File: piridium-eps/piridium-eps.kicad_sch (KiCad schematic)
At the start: 33 parts

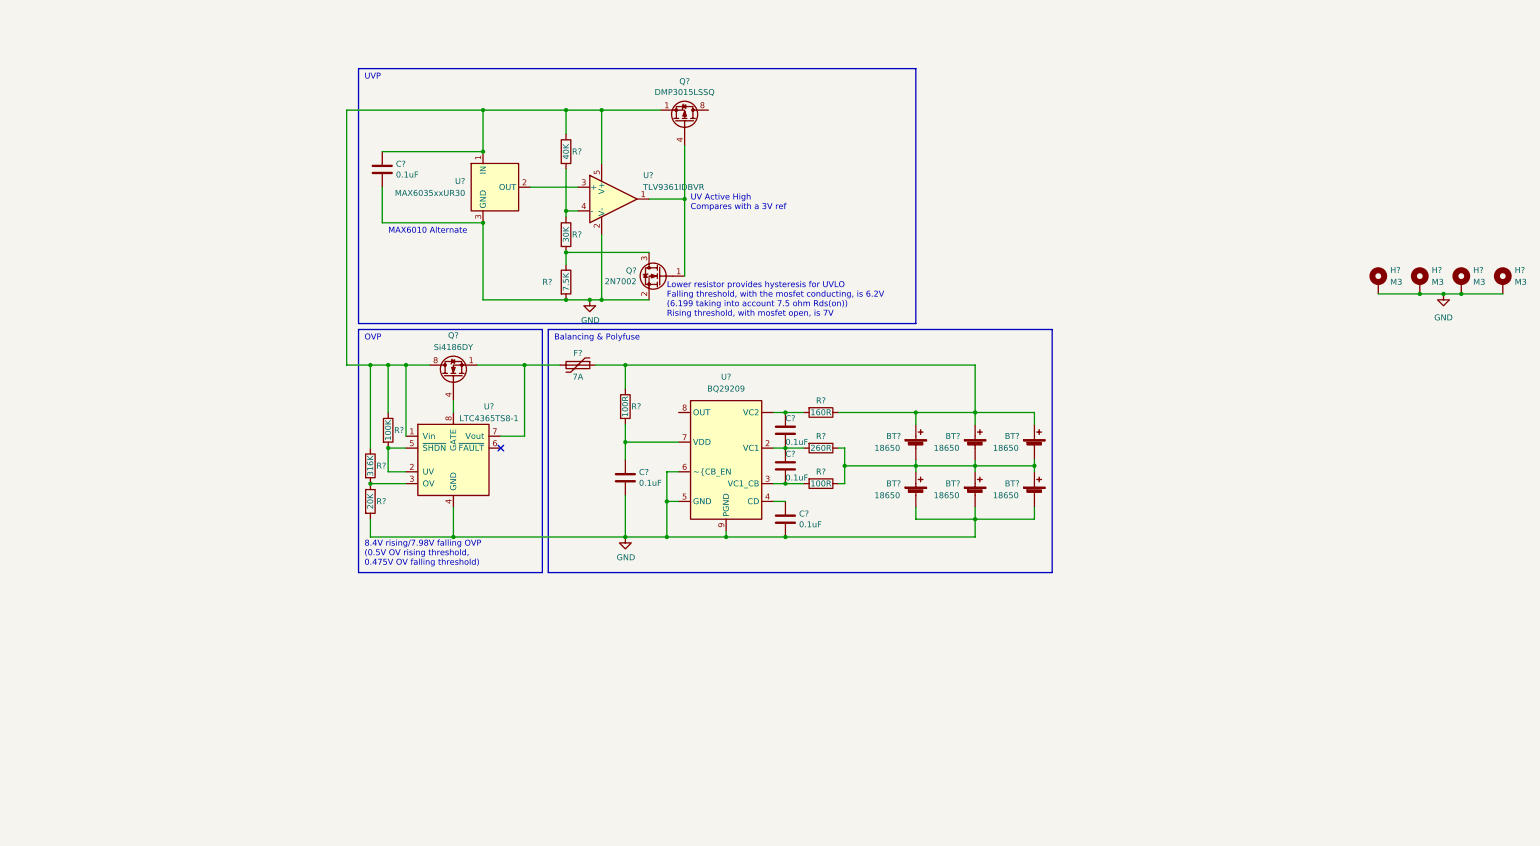
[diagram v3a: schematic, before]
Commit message: add R5460 and small bom edits
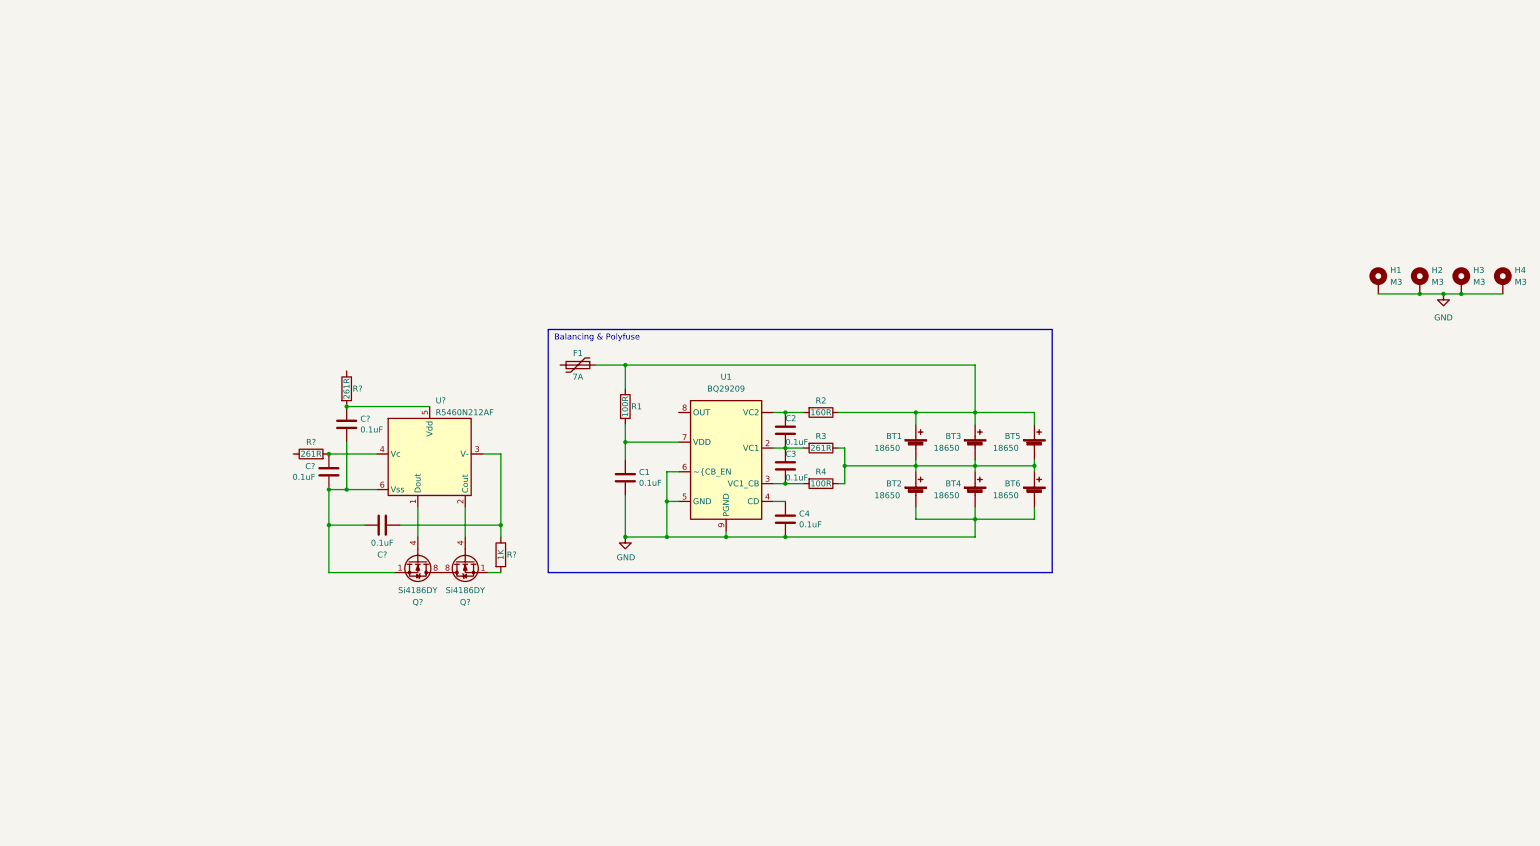
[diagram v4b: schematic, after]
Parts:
- removed C?: 0.1uF, Capacitor_SMD:C_0805_2012Metric, symbol Device:C
- removed Q?: 2N7002, Package_TO_SOT_SMD:SOT-23, symbol Transistor_FET:2N7002
- removed Q?: DMP3015LSSQ, Package_SO:SOIC-8_3.9x4.9mm_P1.27mm, symbol Transistor_FET:IRF7404
- removed Q?: Si4186DY, Package_SO:SOIC-8_3.9x4.9mm_P1.27mm, symbol Transistor_FET:Si4162DY
- removed R?: 30K, Resistor_SMD:R_0805_2012Metric, symbol Device:R
- removed R?: 7.5K, Resistor_SMD:R_0805_2012Metric, symbol Device:R
- removed R?: 100K, Resistor_SMD:R_0805_2012Metric, symbol Device:R
- removed R?: 40K, Resistor_SMD:R_0805_2012Metric, symbol Device:R
- removed R?: 316K, Resistor_SMD:R_0805_2012Metric, symbol Device:R
- removed R?: 20K, Resistor_SMD:R_0805_2012Metric, symbol Device:R
- removed U?: LTC4365TS8-1, Package_TO_SOT_SMD:TSOT-23-8, symbol Power_Management:LTC4365TS8-1
- removed U?: MAX6035xxUR30, Package_TO_SOT_SMD:SOT-23, symbol Reference_Voltage:MAX6035xxUR30
- removed U?: TLV9361IDBVR, Package_TO_SOT_SMD:SOT-23-5, symbol Amplifier_Operational:OPA842xDBV
- added C? (x3): 0.1uF, Capacitor_SMD:C_0805_2012Metric, symbol Device:C
- added Q? (x2): Si4186DY, Package_SO:SOIC-8_3.9x4.9mm_P1.27mm, symbol Transistor_FET:Si4162DY
- added R?: 1K, Resistor_SMD:R_0805_2012Metric, symbol Device:R
- added R? (x2): 261R, Resistor_SMD:R_0805_2012Metric, symbol Device:R
- added U?: R5460N212AF, Package_TO_SOT_SMD:SOT-23-6, symbol piridium-eps:R5460N212AF
- R3: renamed from R?; value 260R -> 261R
- gave numbers to parts that had none: 19
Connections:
- new net: C?.1, R?.2, U?.4 (Vc)
- new net: C?.1, C?.2, C?.2, Q?.1 (S), Q?.2 (S), Q?.3 (S), U?.6 (Vss)
- new net: C?.2, R?.1, U?.3 (V-)
- new net: Q?.1 (S), Q?.2 (S), Q?.3 (S), R?.2
- new net: C?.1, R?.2, U?.5 (Vdd)
- new net: Q?.4 (G), U?.1 (Dout)
- new net: Q?.5 (D), Q?.5 (D), Q?.6 (D), Q?.6 (D), Q?.7 (D), Q?.7 (D), Q?.8 (D), Q?.8 (D)
- new net: Q?.4 (G), U?.2 (Cout)
- no-connect marks 1 -> 0
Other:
- note removed: "8.4V rising/7.98V falling OVP (0.5V OV rising threshold, 0.475V OV falling threshold)"
- note removed: "Lower resistor provides hysteresis for UVLO Falling threshold, with the mosfet conducting, is 6.2V (6.199 taking into account 7.5 ohm Rds(on)) Rising threshold, with mosfet open, is 7V"
- note removed: "MAX6010 Alternate"
- note removed: "OVP"
- note removed: "UV Active High Compares with a 3V ref"
- note removed: "UVP"

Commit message: battery sch finish
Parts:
- added J1: EPS, TerminalBlock_Phoenix:TerminalBlock_Phoenix_PT-1,5-2-3.5-H_1x02_P3.50mm_Horizontal, symbol Connector:Screw_Terminal_01x02
- BT1, BT2, BT3, BT4, BT5, BT6: footprint piridium-eps:18650-weld -> Battery:BatteryHolder_Keystone_1042_1x18650
- gave numbers to parts that had none: 9
- renumbered H1 to MH1, H2 to MH2, H3 to MH3, H4 to MH4
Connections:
- net GND: now also Q2.1 (S), Q2.2 (S), Q2.3 (S), R7.2, J1.2 (Pin_2); no longer BT2.2 (-), BT4.2 (-), BT6.2 (-), C1.2, C4.2, U1.5 (GND), U1.6 (~{CB_EN), U1.9 (PGND)
- net -BATT: now reaches C5.2, C6.2, C7.1, Q1.1 (S), Q1.2 (S), Q1.3 (S), U2.6 (Vss)
- net -BATT: now also BT2.2 (-), BT4.2 (-), BT6.2 (-), C1.2, C4.2, U1.5 (GND), U1.6 (~{CB_EN), U1.9 (PGND)
- net at BT1.2 (-), BT2.1 (+), BT3.2 (-)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: now also R5.1
- net +BATT: now reaches BT1.1 (+), BT3.1 (+), BT5.1 (+), F1.1, R1.1, R2.1
- net +BATT: now also R6.1
- net at F1.2: now also J1.1 (Pin_1)
- no-connect marks 0 -> 1
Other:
- note added: "Balancing"
- note added: "Protection"
- note removed: "Balancing & Polyfuse"
- moved on the sheet: BT1, BT2, BT3, BT4, BT5, BT6, C1, C2, C3, C4, C5, C6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

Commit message: license
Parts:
- BT2: footprint Battery:BatteryHolder_Keystone_1042_1x18650 -> piridium-eps:Keystone_1042_1x18650_Shortpad
- BT3: footprint Battery:BatteryHolder_Keystone_1042_1x18650 -> piridium-eps:Keystone_1042_1x18650_Shortpad2
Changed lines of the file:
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@@
       (effects (font (size 1.27 1.27)) (justify left))
     )
-    (property "Footprint" "Battery:BatteryHolder_Keystone_1042_1x18650" (id 2) (at 166.37 87.376 90)
+    (property "Footprint" "piridium-eps:Keystone_1042_1x18650_Shortpad2" (id 2) (at 166.37 87.376 90)
       (effects (font (size 1.27 1.27)) hide)
     )
@@
       (effects (font (size 1.27 1.27)) (justify left))
     )
-    (property "Footprint" "Battery:BatteryHolder_Keystone_1042_1x18650" (id 2) (at 153.67 97.536 90)
+    (property "Footprint" "piridium-eps:Keystone_1042_1x18650_Shortpad" (id 2) (at 153.67 97.536 90)
       (effects (font (size 1.27 1.27)) hide)
     )
@@
     )
     (path "/ed242fec-6e8d-4cf5-af4a-93636bebd7f7"
-      (reference "BT2") (unit 1) (value "18650") (footprint "Battery:BatteryHolder_Keystone_1042_1x18650")
+      (reference "BT2") (unit 1) (value "18650") (footprint "piridium-eps:Keystone_1042_1x18650_Shortpad")
     )
     (path "/5d447a6e-452c-4990-aba0-6f8a6ee1fb83"
-      (reference "BT3") (unit 1) (value "18650") (footprint "Battery:BatteryHolder_Keystone_1042_1x18650")
+      (reference "BT3") (unit 1) (value "18650") (footprint "piridium-eps:Keystone_1042_1x18650_Shortpad2")
     )
     (path "/503ba92c-dac5-4f0f-8b82-75bf2e24956e"

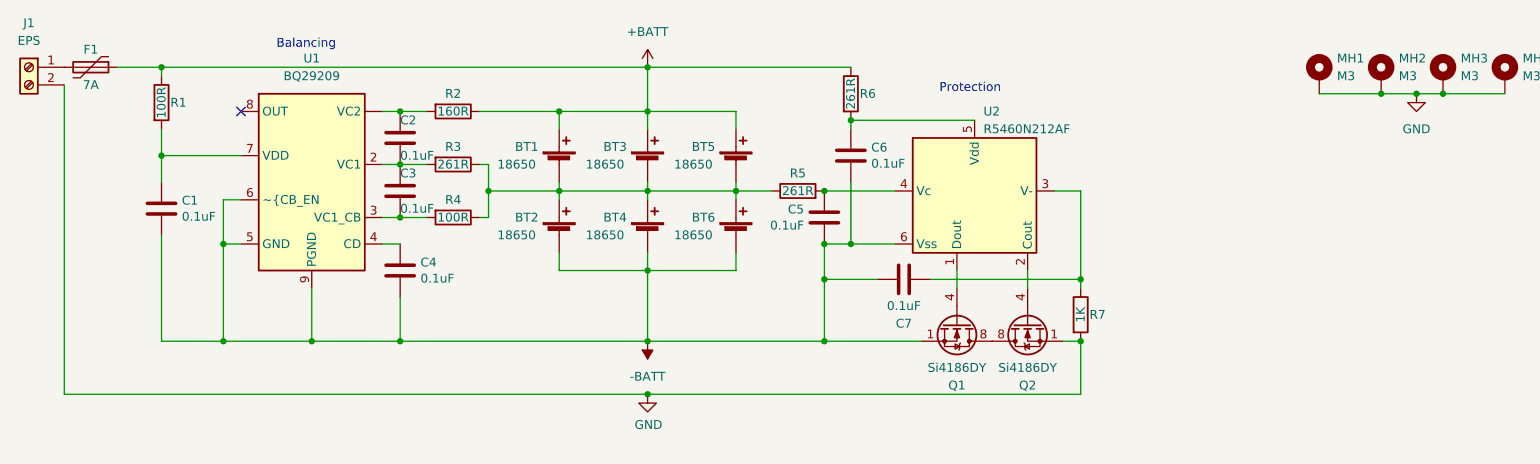
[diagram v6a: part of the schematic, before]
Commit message: finish battery
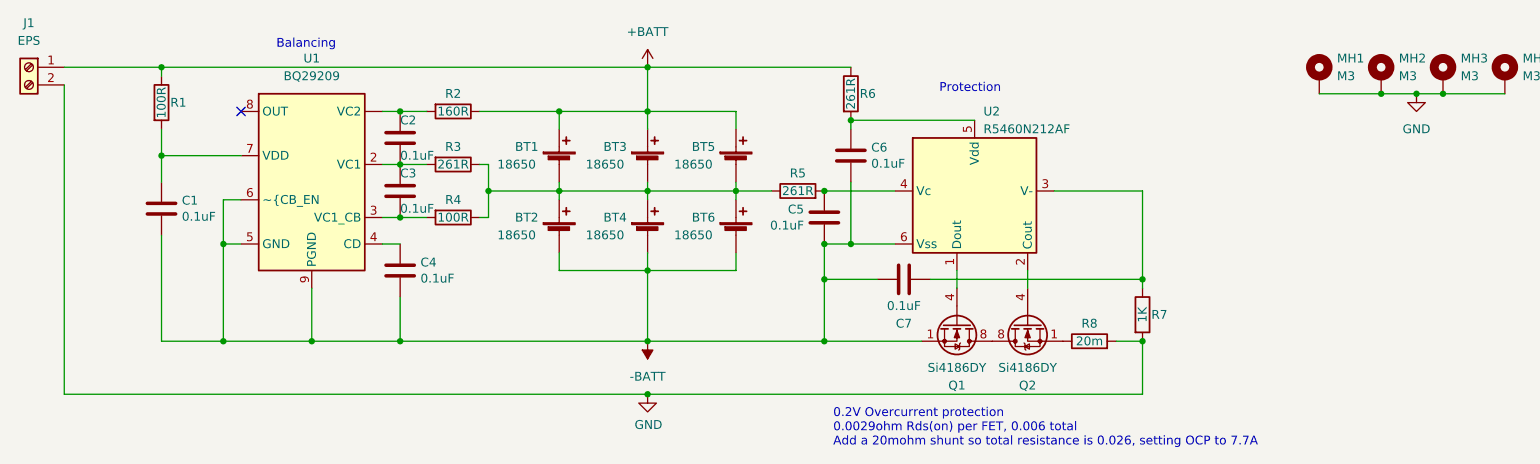
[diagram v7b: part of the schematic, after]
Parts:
- removed F1: 7A, Resistor_SMD:R_1206_3216Metric, symbol Device:Polyfuse
- added R8: 20m, Resistor_SMD:R_2512_6332Metric, symbol Device:R
- BT6: footprint Battery:BatteryHolder_Keystone_1042_1x18650 -> piridium-eps:Keystone_1042_1x18650_Shortpad3
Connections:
- net +BATT: now also J1.1 (Pin_1)
- net GND: now also R8.2; no longer Q2.1 (S), Q2.2 (S), Q2.3 (S)
- new net: Q2.1 (S), Q2.2 (S), Q2.3 (S), R8.1
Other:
- note added: "0.2V Overcurrent protection 0.0029ohm Rds(on) per FET, 0.006 total Add a 20mohm shunt so total resistance is 0.026, setting OCP to 7.7A"
- moved on the sheet: R7
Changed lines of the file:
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@@
   (junction (at 96.52 74.93) (diameter 0) (color 0 0 0 0)
   )
-  (junction (at 228.6 114.3) (diameter 0) (color 0 0 0 0)
+  (junction (at 237.49 114.3) (diameter 0) (color 0 0 0 0)
   )
   (junction (at 153.67 81.28) (diameter 0) (color 0 0 0 0)
@@
   (junction (at 153.67 92.71) (diameter 0) (color 0 0 0 0)
   )
-  (junction (at 228.6 105.41) (diameter 0) (color 0 0 0 0)
+  (junction (at 237.49 105.41) (diameter 0) (color 0 0 0 0)
   )
   (junction (at 166.37 92.71) (diameter 0) (color 0 0 0 0)
@@
     (stroke (width 0) (type default) (color 0 0 0 0))
   )
-  (wire (pts (xy 228.6 121.92) (xy 166.37 121.92))
+  (wire (pts (xy 237.49 121.92) (xy 166.37 121.92))
     (stroke (width 0) (type default) (color 0 0 0 0))
   )
@@
     (stroke (width 0) (type default) (color 0 0 0 0))
   )
-  (wire (pts (xy 228.6 105.41) (xy 228.6 92.71))
-    (stroke (width 0) (type default) (color 0 0 0 0))
-  )
-  (wire (pts (xy 228.6 92.71) (xy 224.79 92.71))
+  (wire (pts (xy 237.49 105.41) (xy 237.49 92.71))
+    (stroke (width 0) (type default) (color 0 0 0 0))
+  )
+  (wire (pts (xy 237.49 92.71) (xy 224.79 92.71))
     (stroke (width 0) (type default) (color 0 0 0 0))
   )
@@
     (stroke (width 0) (type default) (color 0 0 0 0))
   )
+  (wire (pts (xy 233.68 114.3) (xy 237.49 114.3))
+    (stroke (width 0) (type default) (color 0 0 0 0))
+  )
   (wire (pts (xy 191.77 92.71) (xy 201.93 92.71))
     (stroke (width 0) (type default) (color 0 0 0 0))
@@
     (stroke (width 0) (type default) (color 0 0 0 0))
   )
-  (wire (pts (xy 207.01 105.41) (xy 228.6 105.41))
+  (wire (pts (xy 207.01 105.41) (xy 237.49 105.41))
     (stroke (width 0) (type default) (color 0 0 0 0))
   )
@@
     (stroke (width 0) (type default) (color 0 0 0 0))
   )
-  (wire (pts (xy 228.6 105.41) (xy 228.6 106.68))
+  (wire (pts (xy 237.49 105.41) (xy 237.49 106.68))
     (stroke (width 0) (type default) (color 0 0 0 0))
   )
@@
     (stroke (width 0) (type default) (color 0 0 0 0))
   )
-  (wire (pts (xy 226.06 114.3) (xy 228.6 114.3))
-    (stroke (width 0) (type default) (color 0 0 0 0))
-  )
-  (wire (pts (xy 96.52 74.93) (xy 90.17 74.93))
+  (wire (pts (xy 82.55 74.93) (xy 96.52 74.93))
     (stroke (width 0) (type default) (color 0 0 0 0))
   )
@@
     (stroke (width 0) (type default) (color 0 0 0 0))
   )
-  (wire (pts (xy 228.6 114.3) (xy 228.6 121.92))
+  (wire (pts (xy 237.49 114.3) (xy 237.49 121.92))
     (stroke (width 0) (type default) (color 0 0 0 0))
   )
   (wire (pts (xy 96.52 114.3) (xy 105.41 114.3))
     (stroke (width 0) (type default) (color 0 0 0 0))
+  )
+  (text "0.2V Overcurrent protection\n0.0029ohm Rds(on) per FET, 0.006 total\nAdd a 20mohm shunt so total resistance is 0.026, setting OCP to 7.7A"
+    (at 193.04 129.54 0)
+    (effects (font (size 1.27 1.27)) (justify left bottom))
   )
   (text "Balancing" (at 113.03 72.39 0)
@@
     )
     (pin "1")
+  )
+  (symbol (lib_id "Device:R") (at 229.87 114.3 90) (unit 1)
+    (in_bom yes) (on_board yes)
+    (property "Reference" "R8" (id 0) (at 229.87 111.76 90))
+    (property "Value" "20m" (id 1) (at 229.87 114.3 90))
+    (property "Footprint" "Resistor_SMD:R_2512_6332Metric" (id 2) (at 229.87 116.078 90)
+      (effects (font (size 1.27 1.27)) hide)
+    )
+    (property "Datasheet" "~" (id 3) (at 229.87 114.3 0)
+      (effects (font (size 1.27 1.27)) hide)
+    )
+    (pin "1")
+    (pin "2")
   )
   (symbol (lib_id "Device:C") (at 191.77 96.52 0) (mirror y) (unit 1)
@@
     (pin "9")
   )
-  (symbol (lib_id "Device:R") (at 228.6 110.49 0) (unit 1)
-    (in_bom yes) (on_board yes)
-    (property "Reference" "R7" (id 0) (at 229.87 110.49 0)
-      (effects (font (size 1.27 1.27)) (justify left))
-    )
-    (property "Value" "1K" (id 1) (at 228.6 110.49 90))
-    (property "Footprint" "Resistor_SMD:R_0805_2012Metric" (id 2) (at 226.822 110.49 90)
-      (effects (font (size 1.27 1.27)) hide)
-    )
-    (property "Datasheet" "~" (id 3) (at 228.6 110.49 0)
+  (symbol (lib_id "Device:R") (at 237.49 110.49 0) (unit 1)
+    (in_bom yes) (on_board yes)
+    (property "Reference" "R7" (id 0) (at 238.76 110.49 0)
+      (effects (font (size 1.27 1.27)) (justify left))
+    )
+    (property "Value" "1K" (id 1) (at 237.49 110.49 90))
+    (property "Footprint" "Resistor_SMD:R_0805_2012Metric" (id 2) (at 235.712 110.49 90)
+      (effects (font (size 1.27 1.27)) hide)
+    )
+    (property "Datasheet" "~" (id 3) (at 237.49 110.49 0)
       (effects (font (size 1.27 1.27)) hide)
     )
@@
       (effects (font (size 1.27 1.27)) (justify left))
     )
-    (property "Footprint" "Battery:BatteryHolder_Keystone_1042_1x18650" (id 2) (at 179.07 97.536 90)
+    (property "Footprint" "piridium-eps:Keystone_1042_1x18650_Shortpad3" (id 2) (at 179.07 97.536 90)
       (effects (font (size 1.27 1.27)) hide)
     )
@@
     )
     (pin "1")
-  )
-  (symbol (lib_id "Device:Polyfuse") (at 86.36 74.93 270) (unit 1)
-    (in_bom yes) (on_board yes)
-    (property "Reference" "F1" (id 0) (at 86.36 72.39 90))
-    (property "Value" "7A" (id 1) (at 86.36 77.47 90))
-    (property "Footprint" "Resistor_SMD:R_1206_3216Metric" (id 2) (at 81.28 76.2 0)
-      (effects (font (size 1.27 1.27)) (justify left) hide)
-    )
-    (property "Datasheet" "~" (id 3) (at 86.36 74.93 0)
-      (effects (font (size 1.27 1.27)) hide)
-    )
-    (pin "1")
-    (pin "2")
   )
   (symbol (lib_id "Device:R") (at 96.52 80.01 0) (unit 1)
@@
     )
     (path "/4eb7616d-0f7d-445b-b716-8b7048b6092e"
-      (reference "BT6") (unit 1) (value "18650") (footprint "Battery:BatteryHolder_Keystone_1042_1x18650")
+      (reference "BT6") (unit 1) (value "18650") (footprint "piridium-eps:Keystone_1042_1x18650_Shortpad3")
     )
     (path "/a1b43ef3-2e86-4601-8025-c903a8ac3aef"
@@
       (reference "C7") (unit 1) (value "0.1uF") (footprint "Capacitor_SMD:C_0805_2012Metric")
     )
-    (path "/8f683fa3-e1dc-44d7-b56d-98748ee35528"
-      (reference "F1") (unit 1) (value "7A") (footprint "Resistor_SMD:R_1206_3216Metric")
-    )
     (path "/77f310fa-8ef9-4705-8778-95f57a24bcd8"
       (reference "J1") (unit 1) (value "EPS") (footprint "TerminalBlock_Phoenix:TerminalBlock_Phoenix_PT-1,5-2-3.5-H_1x02_P3.50mm_Horizontal")
@@
       (reference "R7") (unit 1) (value "1K") (footprint "Resistor_SMD:R_0805_2012Metric")
     )
+    (path "/1ae8e715-9ddf-4ce5-bfe4-c125ec5de61a"
+      (reference "R8") (unit 1) (value "20m") (footprint "Resistor_SMD:R_2512_6332Metric")
+    )
     (path "/1f17f7a8-633d-4b82-93af-d9fcd1edee05"
